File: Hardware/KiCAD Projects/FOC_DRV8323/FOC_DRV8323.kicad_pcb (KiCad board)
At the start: 4 copper layers, 56.3 x 39.7 mm, 54 parts, among them J101 PZ254-1-13-Z-8.5, J102 PZ254-1-13-Z-8.5, J103 MKS Power, J201 DB301V-3.5-3P-GN-S, J301 DB301V-3.5-3P-GN-S, Q101 HSBB6066, Q201 HSBB6066, Q202 HSBB6066, Q203 HSBB6066, Q204 HSBB6066, Q205 HSBB6066, Q206 HSBB6066, Q301 HSBB6066, Q302 HSBB6066, Q303 HSBB6066, Q304 HSBB6066, Q305 HSBB6066, Q306 HSBB6066, U101 LIS2DE12, U201 DRV8323S, U301 DRV8323S

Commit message: Hardware update
- Removed 5V net as it is not really needed for typical SimpleFOC encoders. This reduces part cost a lot.
- Fixed SPI pin assignment
- Exposed another GPIO pin in place of the +5V pin
- Boards changed to transfer power via the standoff pads instead of a solder connection
- Moved accelerometer to the controller board
- Resistance changes to reduce BOM
- Replaced encoder connection with JST-XH
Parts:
- removed C101, C102: 1u, Capacitor_SMD:C_0603_1608Metric
- removed J103: MKS Power, TestPoint:TestPoint_2Pads_Pitch5.08mm_Drill1.3mm
- removed U101: LIS2DE12, Package_LGA:LGA-12_2x2mm_P0.5mm
- added H101: MountingHole_Pad, MountingHole:MountingHole_3.2mm_M3_Pad_Via, F.Cu at (125.0, 116.8)
- added H102: MountingHole_Pad, MountingHole:MountingHole_3.2mm_M3_Pad_Via, F.Cu at (175.1, 83.2)
- added H103: MountingHole_Pad, MountingHole:MountingHole_3.2mm_M3_Pad_Via, F.Cu at (175.1, 116.8)
- added H104: MountingHole_Pad, MountingHole:MountingHole_3.2mm_M3_Pad_Via, F.Cu at (125.0, 83.2)
- added R106: 1k, Resistor_SMD:R_0603_1608Metric, F.Cu at (150.0, 100.0)
- added TH101: NTCS0805E3103JMT, Resistor_SMD:R_0805_2012Metric, F.Cu at (150.0, 102.0)
- J101: footprint Connector_PinHeader_2.54mm:PinHeader_1x14_P2.54mm_Vertical_SMD_Pin1Right -> Connector_PinHeader_2.54mm:PinHeader_1x13_P2.54mm_Vertical_SMD_Pin1Left
- J102: footprint Connector_PinHeader_2.54mm:PinHeader_1x14_P2.54mm_Vertical_SMD_Pin1Left -> Connector_PinHeader_2.54mm:PinHeader_1x13_P2.54mm_Vertical_SMD_Pin1Right
- R102, R103, R104, R105: value 300m -> 560m
- moved Q101 21.4 mm to (168.9, 113.5), turned to -90 degrees
- moved R101 21.2 mm to (170.0, 108.0), turned to 180 degrees
- moved R105 19.1 mm to (162.0, 113.5), turned to 180 degrees
- moved R104 13.8 mm to (152.5, 113.5), turned to 180 degrees
- moved R103 8.63 mm to (143.0, 113.5), turned to 180 degrees
- moved R102 3.66 mm to (133.5, 113.5), turned to 180 degrees
- moved J101 1.26 mm to (153.8, 88.5)
- moved J102 1.26 mm to (153.8, 111.5)
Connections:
- J101 pad 12: +5V -> unconnected-(J101-Pin_12-Pad12)
- J101 pad 6: /Driver 1/nFAULT -> /Driver 1/ENABLE
- J101 pad 7: /Driver 1/ENABLE -> /Driver 1/nFAULT
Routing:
- net /BrakeChop: track 56.2 -> 26.5 mm
- net /Driver 0/SPI_SDO: track 87.7 -> 75.1 mm
- net /Driver 1/SPI_nSCS: track 43.8 -> 35.2 mm, vias 1 -> 3
- net Net-(J102-Pin_11): track 18.1 -> 25.8 mm
- net /Driver 0/SPI_SCLK: track 76.0 -> 68.9 mm
- net /Driver 1/SOB: track 30.9 -> 37.0 mm
- net /Driver 0/SPI_SDI: track 78.4 -> 72.5 mm, vias 3 -> 2
- net GND: track 0.00 -> 4.57 mm, vias 124 -> 92
- net /Driver 0/SOA: track 57.1 -> 61.0 mm
- net /Driver 0/SPI_nSCS: track 36.5 -> 32.8 mm
- net /Driver 0/INHA: track 30.0 -> 33.7 mm
- net /Driver 0/SOB: track 65.4 -> 61.7 mm
- net /Driver 0/INHC: track 21.1 -> 17.7 mm
- net /Driver 1/INHA: track 18.4 -> 21.7 mm
- net /Driver 0/CAL: track 40.9 -> 37.7 mm
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- removed copper zone on F.Cu, net +3V3
- removed copper zone on B.Cu, net Net-(Q101-D)
- removed copper zone on In1.Cu, net Net-(Q101-D)
- removed copper zone on In2.Cu, net Net-(Q101-D)
- removed copper zone on B.Cu, net Net-(R102-Pad1)
- removed copper zone on In1.Cu, net Net-(R102-Pad1)
- removed copper zone on In2.Cu, net Net-(R102-Pad1)
- removed copper zone on B.Cu, net Net-(R103-Pad1)
- removed copper zone on In1.Cu, net Net-(R103-Pad1)
- removed copper zone on In2.Cu, net Net-(R103-Pad1)
- removed copper zone on B.Cu, net Net-(R104-Pad1)
- removed copper zone on In1.Cu, net Net-(R104-Pad1)
- removed copper zone on In2.Cu, net Net-(R104-Pad1)
- removed copper zone on In1.Cu, net VM
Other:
- outline, holes or cut-outs redrawn
- board text added: "Board Therm"
- board text removed: "- +"
- board text removed: "Accel (G)"
- board text removed: "LIS2DE12"
- board text removed: "PCB Temp"
- board text removed: "POWER IN"

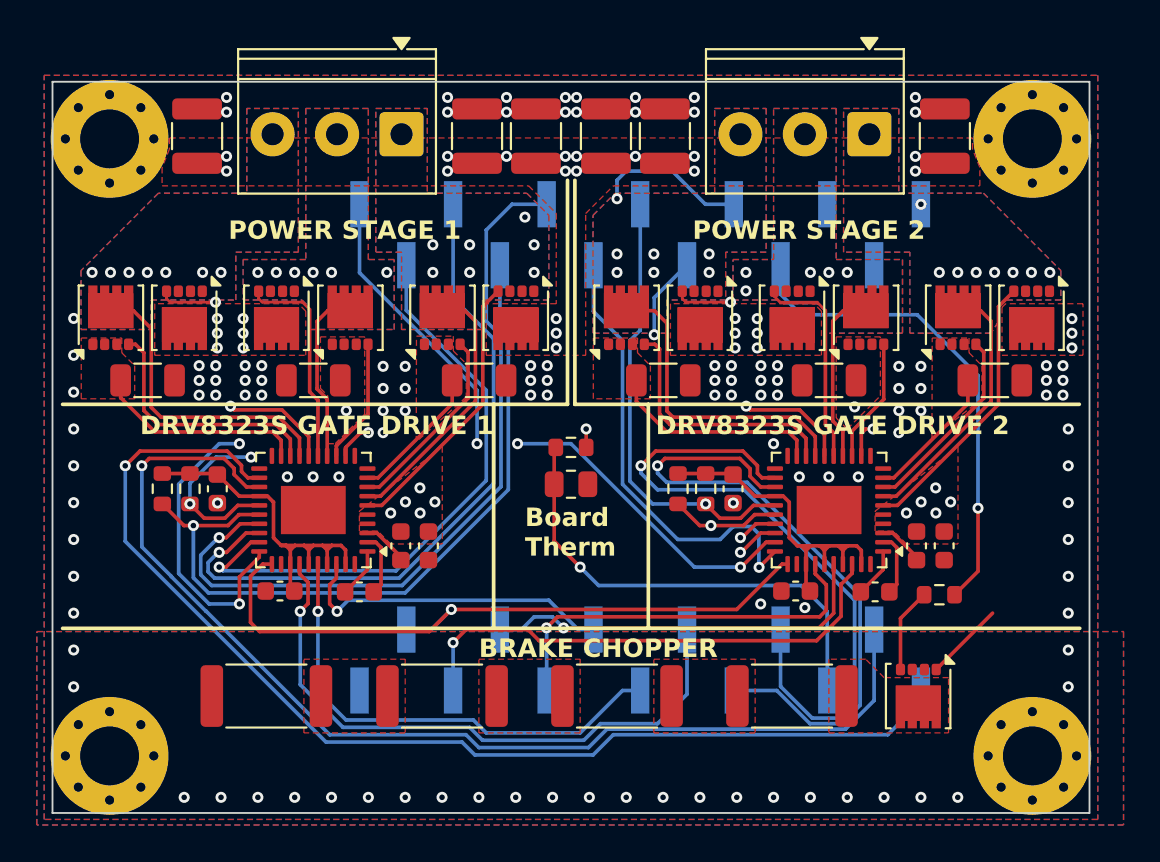
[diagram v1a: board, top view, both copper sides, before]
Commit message: Driver redesign to allow 8323H and 8323S
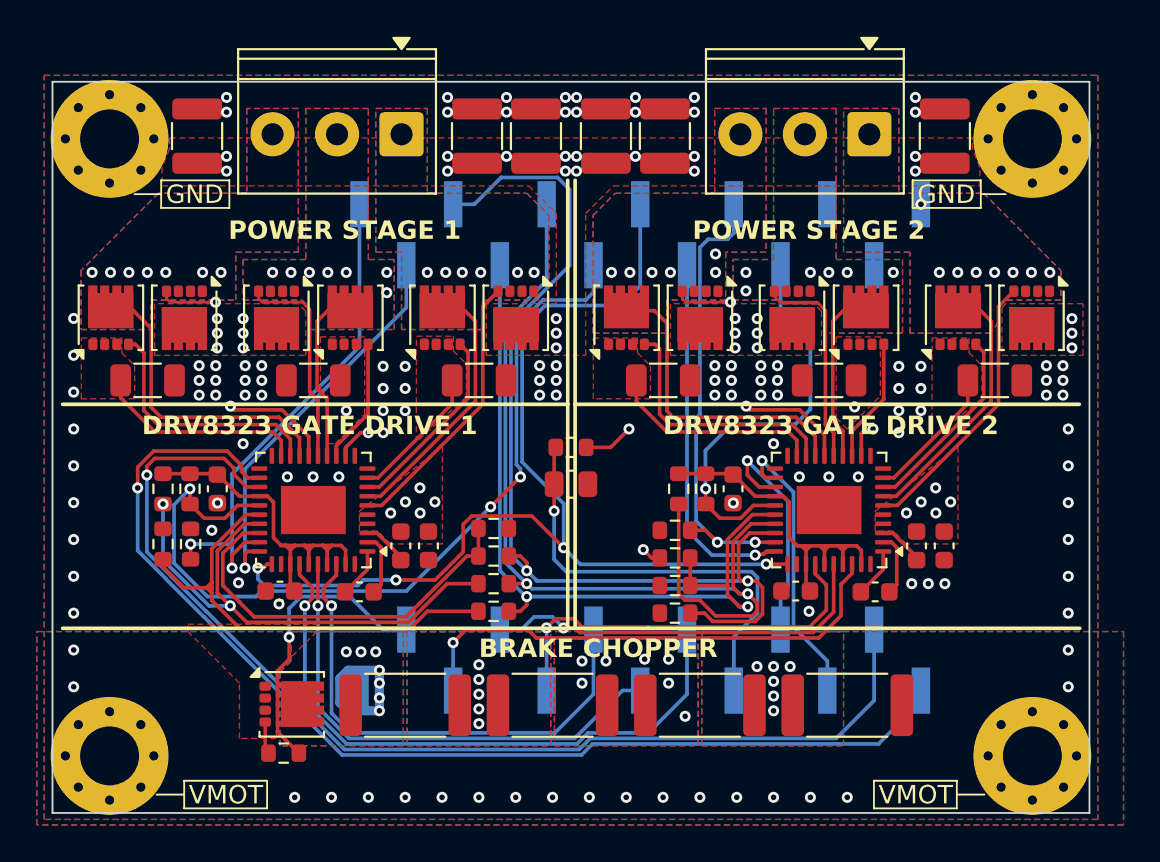
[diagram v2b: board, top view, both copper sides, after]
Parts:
- added R107: 1k, Resistor_SMD:R_0603_1608Metric, F.Cu at (155.7, 106.0)
- added R108: 0, Resistor_SMD:R_0603_1608Metric, F.Cu at (145.8, 105.9)
- added R109: 0, Resistor_SMD:R_0603_1608Metric, F.Cu at (145.8, 108.9)
- added R110: 0, Resistor_SMD:R_0603_1608Metric, F.Cu at (145.8, 107.4)
- added R206: 47k, Resistor_SMD:R_0603_1608Metric, F.Cu at (127.8, 105.2)
- added R207: 0, Resistor_SMD:R_0603_1608Metric, F.Cu at (127.8, 102.2)
- added R209: 47k, Resistor_SMD:R_0603_1608Metric, F.Cu at (129.3, 105.2)
- added R306: 47k, Resistor_SMD:R_0603_1608Metric, F.Cu at (155.7, 107.5)
- added R307: 0, Resistor_SMD:R_0603_1608Metric, F.Cu at (155.8, 102.2)
- added R309: 47k, Resistor_SMD:R_0603_1608Metric, F.Cu at (155.7, 104.5)
- R201, R301: value 1k -> 75k
- moved R101 36.6 mm to (134.4, 116.6)
- moved Q101 34.0 mm to (134.8, 113.9), turned to 0 degrees
- moved R102 31.5 mm to (165.0, 114.0), turned to 0 degrees
- moved R105 21.0 mm to (141.0, 114.0), turned to 0 degrees
- moved R201 18.1 mm to (145.8, 104.4), turned to 0 degrees
- moved R103 14.0 mm to (157.0, 114.0), turned to 0 degrees
- moved R301 6.76 mm to (155.7, 109.0), turned to 180 degrees
- moved R104 3.54 mm to (149.0, 114.0), turned to 0 degrees
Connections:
- net /Driver 0/INHA renamed /HDR2_08_Drv0INHA
- net /Driver 0/INHB renamed /HDR2_07_Drv0INHB
- net /Driver 0/INHC renamed /HDR2_06_Drv0INHC
- net /Driver 0/SOA renamed /HDR2_12_Drv0SOA
- net /Driver 0/SOB renamed /HDR2_13_Drv0SOB
- net /Driver 1/INHA renamed /HDR2_05_Drv1INHA
- net /Driver 1/INHB renamed /HDR2_04_Drv1INHB
- net /Driver 1/INHC renamed /HDR2_03_Drv1INHC
- J101 pad 1: /Driver 1/SPI_nSCS -> /HDR1_01_Drv0Select
- J101 pad 10: /BrakeChop -> /HDR1_10_Drv1Fault
- J101 pad 2: /Driver 0/SPI_nSCS -> /HDR1_02_Drv0Enable
- J101 pad 3: /Driver 0/SPI_SCLK -> /HDR1_03_SCLK
- J101 pad 4: /Driver 0/SPI_SDO -> /HDR1_04_MISO
- J101 pad 5: /Driver 0/SPI_SDI -> /HDR1_05_MOSI
- J101 pad 6: /Driver 1/ENABLE -> /HDR1_06_Drv0Fault
- J101 pad 7: /Driver 1/nFAULT -> /HDR1_07_Calibrate
- J101 pad 8: /Driver 0/nFAULT -> /HDR1_08_Drv1Enable
- J101 pad 9: /Driver 0/ENABLE -> /HDR1_09_Drv1Select
- J102 pad 10: /Driver 1/SOB -> /HDR2_10_Drv1SOA
- J102 pad 11: Net-(J102-Pin_11) -> /HDR2_11_Drv1SOB
- J102 pad 2: /Driver 0/CAL -> /HDR2_02_BrakeChop
- J102 pad 9: /Driver 1/SOA -> /HDR2_09_Thermistor
- R101 pad 1: /BrakeChop -> /HDR2_02_BrakeChop
- R106 pad 1: Net-(J102-Pin_11) -> /HDR2_09_Thermistor
- R201 pad 1: /Driver 0/DVDD -> /Driver 0/SCLK/VDS
- R201 pad 2: /Driver 0/SPI_SDO -> GND
- R202 pad 2: /Driver 0/nFAULT -> /HDR1_06_Drv0Fault
- R301 pad 1: /Driver 1/DVDD -> /HDR1_03_SCLK
- R301 pad 2: /Driver 0/SPI_SDO -> GND
- R302 pad 2: /Driver 1/nFAULT -> /HDR1_10_Drv1Fault
- TH101 pad 1: Net-(J102-Pin_11) -> /HDR2_09_Thermistor
- U201 pad 25: /Driver 0/nFAULT -> /HDR1_06_Drv0Fault
- U201 pad 26: /Driver 0/SPI_SDO -> /Driver 0/SDO/MODE
- U201 pad 27: /Driver 0/SPI_SDI -> /Driver 0/SDI/IDRIVE
- U201 pad 28: /Driver 0/SPI_SCLK -> /Driver 0/SCLK/VDS
- U201 pad 29: /Driver 0/SPI_nSCS -> /HDR1_01_Drv0Select
- U201 pad 30: /Driver 0/ENABLE -> /HDR1_02_Drv0Enable
- U201 pad 31: /Driver 0/CAL -> /HDR1_07_Calibrate
- U301 pad 22: /Driver 1/SOB -> /HDR2_11_Drv1SOB
- U301 pad 23: /Driver 1/SOA -> /HDR2_10_Drv1SOA
- U301 pad 25: /Driver 1/nFAULT -> /HDR1_10_Drv1Fault
- U301 pad 26: /Driver 0/SPI_SDO -> /HDR1_04_MISO
- U301 pad 27: /Driver 0/SPI_SDI -> /HDR1_05_MOSI
- U301 pad 28: /Driver 0/SPI_SCLK -> /HDR1_03_SCLK
- U301 pad 29: /Driver 1/SPI_nSCS -> /HDR1_09_Drv1Select
- U301 pad 30: /Driver 1/ENABLE -> /HDR1_08_Drv1Enable
- U301 pad 31: /Driver 0/CAL -> /HDR1_07_Calibrate
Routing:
- net /Driver 0/SPI_SDO: track 75.1 -> 0.00 mm, vias 2 -> 0
- net /Driver 0/SPI_SDI: track 72.5 -> 0.00 mm, vias 2 -> 0
- net /Driver 0/SPI_SCLK: track 68.9 -> 0.00 mm, vias 2 -> 0
- net /HDR1_07_Calibrate: track 0.00 -> 58.5 mm, vias 0 -> 4
- net /HDR1_03_SCLK: track 0.00 -> 54.7 mm, vias 0 -> 2
- net /HDR1_05_MOSI: track 0.00 -> 52.2 mm, vias 0 -> 2
- net /Driver 0/ENABLE: track 51.8 -> 0.00 mm, vias 3 -> 0
- net /HDR1_06_Drv0Fault: track 0.00 -> 46.5 mm, vias 0 -> 3
- net /HDR1_04_MISO: track 0.00 -> 43.5 mm, vias 0 -> 2
- net /Driver 0/nFAULT: track 38.7 -> 0.00 mm, vias 3 -> 0
- net /Driver 0/CAL: track 37.7 -> 0.00 mm, vias 1 -> 0
- net /Driver 1/SOB: track 37.0 -> 0.00 mm, vias 1 -> 0
- net /Driver 1/SOA: track 35.6 -> 0.00 mm, vias 1 -> 0
- net /Driver 1/SPI_nSCS: track 35.2 -> 0.00 mm, vias 3 -> 0
- net /Driver 0/SPI_nSCS: track 32.8 -> 0.00 mm, vias 1 -> 0
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- added copper zone on B.Cu, net Net-(Q101-D)
- added copper zone on B.Cu, net Net-(R102-Pad1)
- added copper zone on B.Cu, net Net-(R103-Pad1)
- added copper zone on B.Cu, net Net-(R104-Pad1)
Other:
- board text added: "DRV8323 GATE DRIVE 1"
- board text added: "DRV8323 GATE DRIVE 2"
- board text added: "GND"
- board text added: "VMOT"
- board text removed: "Board Therm"
- board text removed: "DRV8323S GATE DRIVE 1"
- board text removed: "DRV8323S GATE DRIVE 2"
